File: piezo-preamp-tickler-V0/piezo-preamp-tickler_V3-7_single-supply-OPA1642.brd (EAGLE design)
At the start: 100.3 x 20.1 mm, 61 parts, among them IC1 OPA1642, IC4 BQ297X, IC5 SC4503, IC6 TPS7A49, J1 HEADPHONES, J2 PHONE, J3 Mixer, J5 Battery, Q1 MMBFJ201, SW1 SWITCH_DPDT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

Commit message: Add files via upload
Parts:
- L2: device SparkFun-Passives:0603 -> SparkFun-Passives:CR54
- moved R22 3.40 mm to (63.8, 1.80)
- moved R21 3.20 mm to (19.5, 5.92)
- moved C16 2.40 mm to (23.8, 5.20)
- moved IC6 2.40 mm to (21.2, 10.8)
- moved R23 2.10 mm to (67.0, 2.10), turned to 90 degrees
- moved IC4 1.40 mm to (69.7, 2.09)
- moved R19 1.39 mm to (53.1, 14.7)
- moved R13 1.28 mm to (48.1, 11.6)
- moved R15 1.26 mm to (58.9, 7.80)
- moved R17 1.08 mm to (53.0, 11.4)
- moved C10 0.92 mm to (26.3, 12.9)
- moved R6 0.45 mm to (49.6, 16.0)
- moved C11 0.41 mm to (46.8, 15.2)
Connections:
- removed net N$15: C6.1, J4.VBUS, U$1.4
- removed net V+: C10.1, C11.1, C15.1, D2.C, IC6.5, IC6.8, LED2.A, R18.2
- new net +5V: C6.1, J4.VBUS, LED2.A, U$1.4
- new net VUSB: C10.1, C11.1, C15.1, D2.C, IC6.5, IC6.8, R18.2
- net N$32: now also L2.P$2; no longer L2.2
- net VBAT: now also L2.P$1; no longer L2.1
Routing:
- net V+: track 95.7 -> 0.00 mm, vias 4 -> 0
- net VUSB: track 0.00 -> 77.0 mm, vias 0 -> 2
- net +5V: track 0.00 -> 51.0 mm, vias 0 -> 1
- net N$19: track 75.5 -> 26.5 mm, vias 2 -> 4
- net N$26: track 105.0 -> 58.9 mm, vias 0 -> 5
- net N$15: track 28.2 -> 0.00 mm, vias 2 -> 0
- net GND: track 266.2 -> 238.7 mm, vias 9 -> 6
- net N$8: track 42.4 -> 65.9 mm, vias 2 -> 0
- net N$17: track 100.8 -> 120.0 mm, vias 2 -> 0
- net N$30: track 54.1 -> 69.7 mm, vias 4 -> 5
- net USBGND: track 101.2 -> 86.7 mm
- net N$4: track 128.7 -> 119.1 mm
- net BATGND: track 35.9 -> 28.3 mm, vias 3 -> 4
- net VBAT: track 134.0 -> 127.4 mm, vias 7 -> 4
- net N$16: track 45.1 -> 41.4 mm, vias 7 -> 3
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
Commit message: Add files via upload
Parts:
- IC1: value OPA1642 -> TL072D
- moved IC1 0.22 mm to (32.6, 11.5)
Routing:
- net N$11: track 24.6 -> 66.5 mm, vias 3 -> 1
- net SELECT: track 31.5 -> 56.6 mm
- net N$29: track 38.5 -> 63.2 mm, vias 4 -> 2
- net N$8: track 65.9 -> 42.8 mm, vias 0 -> 2
- net N$30: track 69.7 -> 47.1 mm, vias 5 -> 4
- net N$17: track 120.0 -> 100.0 mm, vias 0 -> 2
- net N$19: track 26.5 -> 43.0 mm, vias 4 -> 0
- net N$4: track 119.1 -> 132.7 mm, vias 0 -> 2
- net VBAT: track 127.4 -> 139.5 mm
- net VUSB: track 77.0 -> 65.4 mm, vias 2 -> 5
- net GND: track 238.7 -> 249.9 mm, vias 6 -> 8
- net +5V: track 51.0 -> 61.7 mm
- net N$16: track 41.4 -> 31.9 mm, vias 3 -> 1
- net BATGND: track 28.3 -> 36.3 mm
- net N$1: track 38.8 -> 45.9 mm, vias 0 -> 2
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
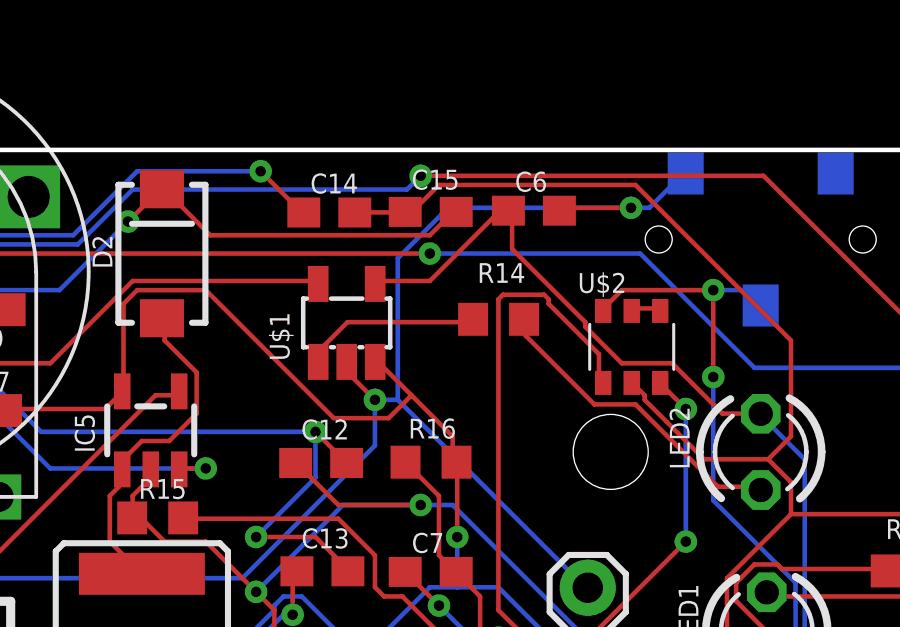
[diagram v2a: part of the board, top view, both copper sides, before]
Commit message: Add files via upload
IC names changed according to convention
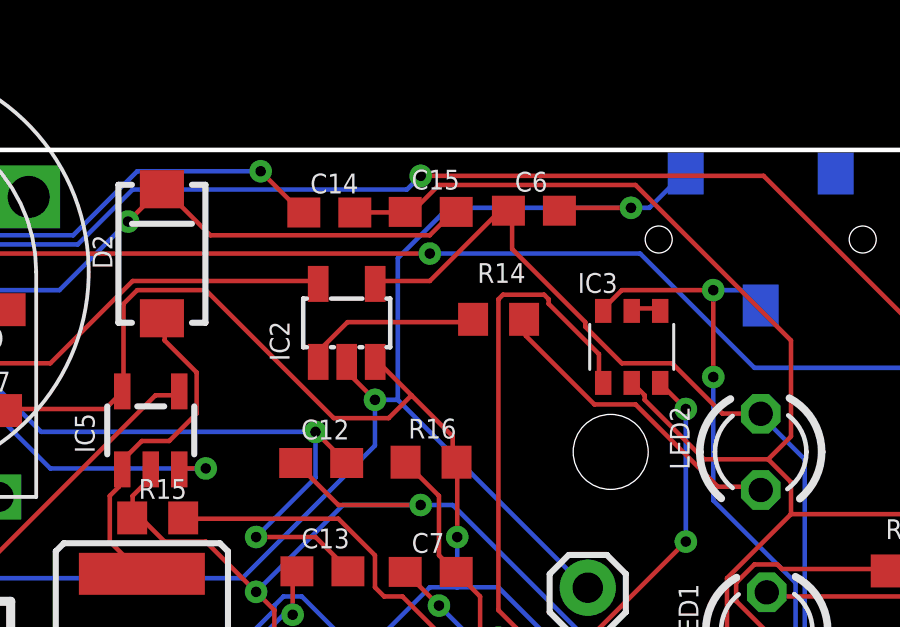
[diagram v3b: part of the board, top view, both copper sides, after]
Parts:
- renumbered U$1 to IC2, U$2 to IC3
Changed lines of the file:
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@@
 <attribute name="VALUE" x="47.29" y="6.87" size="0.6604" layer="21" font="vector" ratio="15"/>
 </element>
-<element name="U$1" library="CMU-ArtFab" package="SOT-23-5" value="MCP73831" x="65.2" y="14.3" smashed="yes">
+<element name="IC2" library="CMU-ArtFab" package="SOT-23-5" value="MCP73831" x="65.2" y="14.3" smashed="yes">
 <attribute name="NAME" x="63.295" y="13.03" size="0.6604" layer="25" font="vector" ratio="15" rot="R90"/>
 <attribute name="VALUE" x="67.64" y="11.63" size="0.6604" layer="27" font="vector" ratio="15" rot="R90"/>
 </element>
-<element name="U$2" library="CMU-ArtFab" package="SOT457R_PHILIPS" value="QS6K1" x="74.7" y="13.5" smashed="yes">
+<element name="IC3" library="CMU-ArtFab" package="SOT457R_PHILIPS" value="QS6K1" x="74.7" y="13.5" smashed="yes">
 <attribute name="NAME" x="72.9" y="15.3" size="0.6604" layer="25" font="vector" ratio="15"/>
 <attribute name="VALUE" x="72.6" y="11.1" size="0.6604" layer="27" font="vector" ratio="15"/>
@@
 <contactref element="C14" pad="2"/>
 <contactref element="C15" pad="2"/>
-<contactref element="U$2" pad="2"/>
+<contactref element="IC3" pad="2"/>
 <contactref element="R15" pad="1"/>
 <contactref element="R22" pad="1"/>
@@
 <contactref element="L2" pad="P$1"/>
 <contactref element="C8" pad="1"/>
-<contactref element="U$1" pad="3"/>
+<contactref element="IC2" pad="3"/>
 <contactref element="C16" pad="1"/>
 <wire x1="3.3528" y1="2.8956" x2="3.048" y2="2.8956" width="0.1524" layer="1"/>
@@
 <contactref element="IC4" pad="4"/>
 <contactref element="C7" pad="1"/>
-<contactref element="U$2" pad="6"/>
+<contactref element="IC3" pad="6"/>
 <wire x1="74.3712" y1="15.3924" x2="73.7616" y2="14.7828" width="0.1524" layer="1"/>
 <wire x1="77.4192" y1="15.3924" x2="74.3712" y2="15.3924" width="0.1524" layer="1"/>
@@
 </signal>
 <signal name="N$21">
-<contactref element="U$1" pad="5"/>
+<contactref element="IC2" pad="5"/>
 <contactref element="R13" pad="2"/>
 <wire x1="49.9872" y1="11.7348" x2="49.0728" y2="11.7348" width="0.1524" layer="1"/>
@@
 <signal name="N$25">
 <contactref element="R14" pad="2"/>
-<contactref element="U$1" pad="1"/>
+<contactref element="IC2" pad="1"/>
 <wire x1="65.2272" y1="14.3256" x2="69.342" y2="14.3256" width="0.1524" layer="1"/>
 <wire x1="64.3128" y1="13.4112" x2="65.2272" y2="14.3256" width="0.1524" layer="1"/>
@@
 </signal>
 <signal name="N$23">
-<contactref element="U$2" pad="5"/>
-<contactref element="U$2" pad="4"/>
+<contactref element="IC3" pad="5"/>
+<contactref element="IC3" pad="4"/>
 <wire x1="75.5904" y1="14.7828" x2="74.8284" y2="14.7828" width="0.1524" layer="1"/>
 <wire x1="74.8284" y1="14.7828" x2="74.7" y2="14.7" width="0.1524" layer="1"/>
@@
 </signal>
 <signal name="N$27">
-<contactref element="U$2" pad="1"/>
+<contactref element="IC3" pad="1"/>
 <contactref element="IC4" pad="3"/>
 <contactref element="R23" pad="2"/>
@@
 </signal>
 <signal name="N$31">
-<contactref element="U$2" pad="3"/>
+<contactref element="IC3" pad="3"/>
 <contactref element="IC4" pad="2"/>
 <contactref element="R22" pad="2"/>
@@
 <contactref element="C6" pad="2"/>
 <contactref element="J4" pad="GND"/>
-<contactref element="U$1" pad="2"/>
+<contactref element="IC2" pad="2"/>
 <contactref element="C16" pad="2"/>
 <contactref element="SW3" pad="P$1"/>
@@
 <contactref element="J4" pad="VBUS"/>
 <contactref element="C6" pad="1"/>
-<contactref element="U$1" pad="4"/>
+<contactref element="IC2" pad="4"/>
 <contactref element="LED2" pad="A"/>
 <wire x1="70.2564" y1="17.9832" x2="70.5612" y2="17.9832" width="0.1524" layer="1"/>
